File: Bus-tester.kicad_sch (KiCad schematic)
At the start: 79 parts, among them J1 POWER, J10 In_Reg, J11 Out_Reg, J12 POWER, J2 POWER, J3 C1_out, J4 C2_out, J5 C3_out, J6 C4_out, J7 Out_sw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

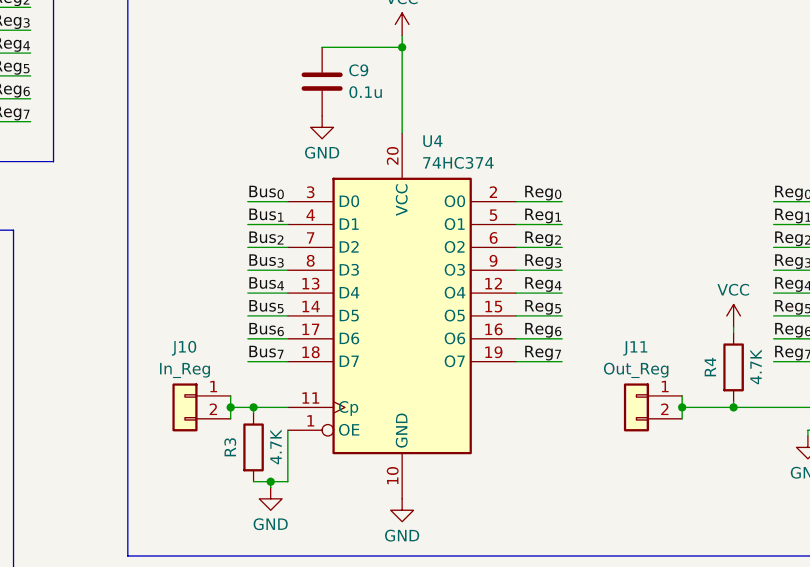
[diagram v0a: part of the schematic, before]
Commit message: optimize routing for register chip
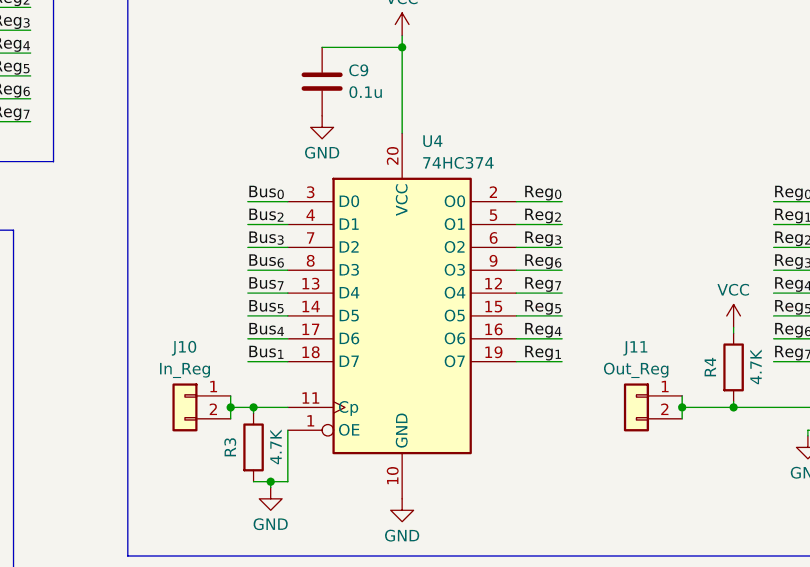
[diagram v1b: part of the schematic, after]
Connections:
- net Bus_{1}: now also U4.18 (D7); no longer U4.4 (D1)
- net Bus_{2}: now also U4.4 (D1); no longer U4.7 (D2)
- net Bus_{3}: now also U4.7 (D2); no longer U4.8 (D3)
- net Bus_{4}: now also U4.17 (D6); no longer U4.13 (D4)
- net Bus_{6}: now also U4.8 (D3); no longer U4.17 (D6)
- net Bus_{7}: now also U4.13 (D4); no longer U4.18 (D7)
- net Reg_{1}: now also U4.19 (O7); no longer U4.5 (O1)
- net Reg_{2}: now also U4.5 (O1); no longer U4.6 (O2)
- net Reg_{3}: now also U4.6 (O2); no longer U4.9 (O3)
- net Reg_{4}: now also U4.16 (O6); no longer U4.12 (O4)
- net Reg_{6}: now also U4.9 (O3); no longer U4.16 (O6)
- net Reg_{7}: now also U4.12 (O4); no longer U4.19 (O7)
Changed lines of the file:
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@@
     (effects (font (size 1.27 1.27)) (justify right bottom))
   )
-  (label "Bus_{1}" (at 184.15 93.345 0) (fields_autoplaced)
-    (effects (font (size 1.27 1.27)) (justify left bottom))
-  )
-  (label "Reg_{7}" (at 219.075 108.585 180) (fields_autoplaced)
-    (effects (font (size 1.27 1.27)) (justify right bottom))
-  )
-  (label "Reg_{2}" (at 219.075 95.885 180) (fields_autoplaced)
+  (label "Bus_{2}" (at 184.15 93.345 0) (fields_autoplaced)
+    (effects (font (size 1.27 1.27)) (justify left bottom))
+  )
+  (label "Reg_{1}" (at 219.075 108.585 180) (fields_autoplaced)
+    (effects (font (size 1.27 1.27)) (justify right bottom))
+  )
+  (label "Reg_{3}" (at 219.075 95.885 180) (fields_autoplaced)
     (effects (font (size 1.27 1.27)) (justify right bottom))
   )
@@
     (effects (font (size 1.27 1.27)) (justify right bottom))
   )
-  (label "Bus_{2}" (at 184.15 95.885 0) (fields_autoplaced)
-    (effects (font (size 1.27 1.27)) (justify left bottom))
-  )
-  (label "Reg_{1}" (at 219.075 93.345 180) (fields_autoplaced)
+  (label "Bus_{3}" (at 184.15 95.885 0) (fields_autoplaced)
+    (effects (font (size 1.27 1.27)) (justify left bottom))
+  )
+  (label "Reg_{2}" (at 219.075 93.345 180) (fields_autoplaced)
     (effects (font (size 1.27 1.27)) (justify right bottom))
   )
@@
     (effects (font (size 1.27 1.27)) (justify left bottom))
   )
-  (label "Bus_{3}" (at 184.15 98.425 0) (fields_autoplaced)
+  (label "Bus_{6}" (at 184.15 98.425 0) (fields_autoplaced)
     (effects (font (size 1.27 1.27)) (justify left bottom))
   )
@@
     (effects (font (size 1.27 1.27)) (justify left bottom))
   )
-  (label "Reg_{4}" (at 219.075 100.965 180) (fields_autoplaced)
+  (label "Reg_{7}" (at 219.075 100.965 180) (fields_autoplaced)
     (effects (font (size 1.27 1.27)) (justify right bottom))
   )
@@
     (effects (font (size 1.27 1.27)) (justify left bottom))
   )
-  (label "Reg_{6}" (at 219.075 106.045 180) (fields_autoplaced)
+  (label "Reg_{4}" (at 219.075 106.045 180) (fields_autoplaced)
     (effects (font (size 1.27 1.27)) (justify right bottom))
   )
@@
     (effects (font (size 1.27 1.27)) (justify left bottom))
   )
-  (label "Bus_{4}" (at 184.15 100.965 0) (fields_autoplaced)
+  (label "Bus_{7}" (at 184.15 100.965 0) (fields_autoplaced)
     (effects (font (size 1.27 1.27)) (justify left bottom))
   )
@@
     (effects (font (size 1.27 1.27)) (justify left bottom))
   )
-  (label "Bus_{7}" (at 184.15 108.585 0) (fields_autoplaced)
+  (label "Bus_{1}" (at 184.15 108.585 0) (fields_autoplaced)
     (effects (font (size 1.27 1.27)) (justify left bottom))
   )
@@
     (effects (font (size 1.27 1.27)) (justify left bottom))
   )
-  (label "Bus_{6}" (at 184.15 106.045 0) (fields_autoplaced)
+  (label "Bus_{4}" (at 184.15 106.045 0) (fields_autoplaced)
     (effects (font (size 1.27 1.27)) (justify left bottom))
   )
@@
     (effects (font (size 1.27 1.27)) (justify right bottom))
   )
-  (label "Reg_{3}" (at 219.075 98.425 180) (fields_autoplaced)
-    (effects (font (size 1.27 1.27)) (justify right bottom))
-  )
+  (label "Reg_{6}" (at 219.075 98.425 180) (fields_autoplaced)
+    (effects (font (size 1.27 1.27)) (justify right bottom))
+  )
